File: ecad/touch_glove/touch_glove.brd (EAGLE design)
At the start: 78.3 x 40.6 mm, 173 parts, among them Q1 MCH3474 4A/30V, Q2 MCH3474 4A/30V, Q3 MCH3474 4A/30V, Q4 MCH3474 4A/30V, Q5 MCH3474 4A/30V, Q6 MCH3474 4A/30V, SW1 4A/28V, Y2 16 MHz

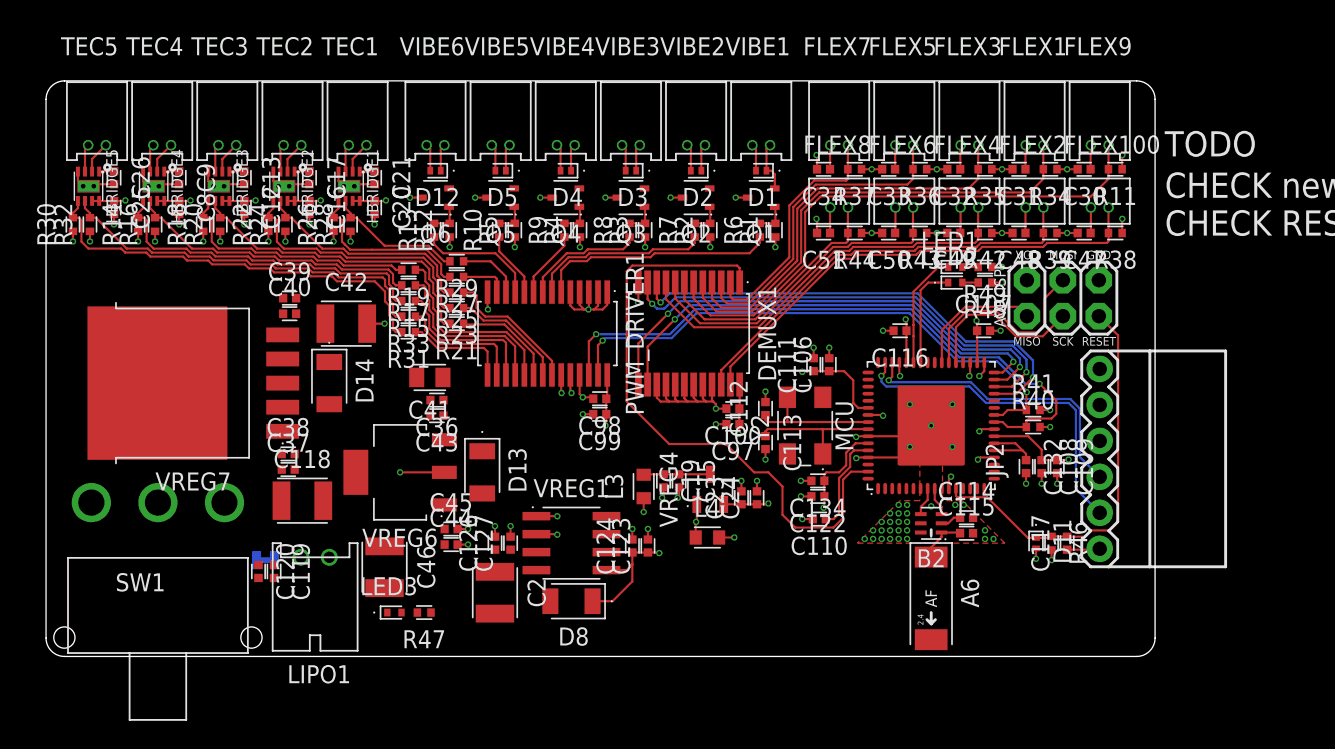
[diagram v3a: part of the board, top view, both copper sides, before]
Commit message: Add option to use two different analog voltages.
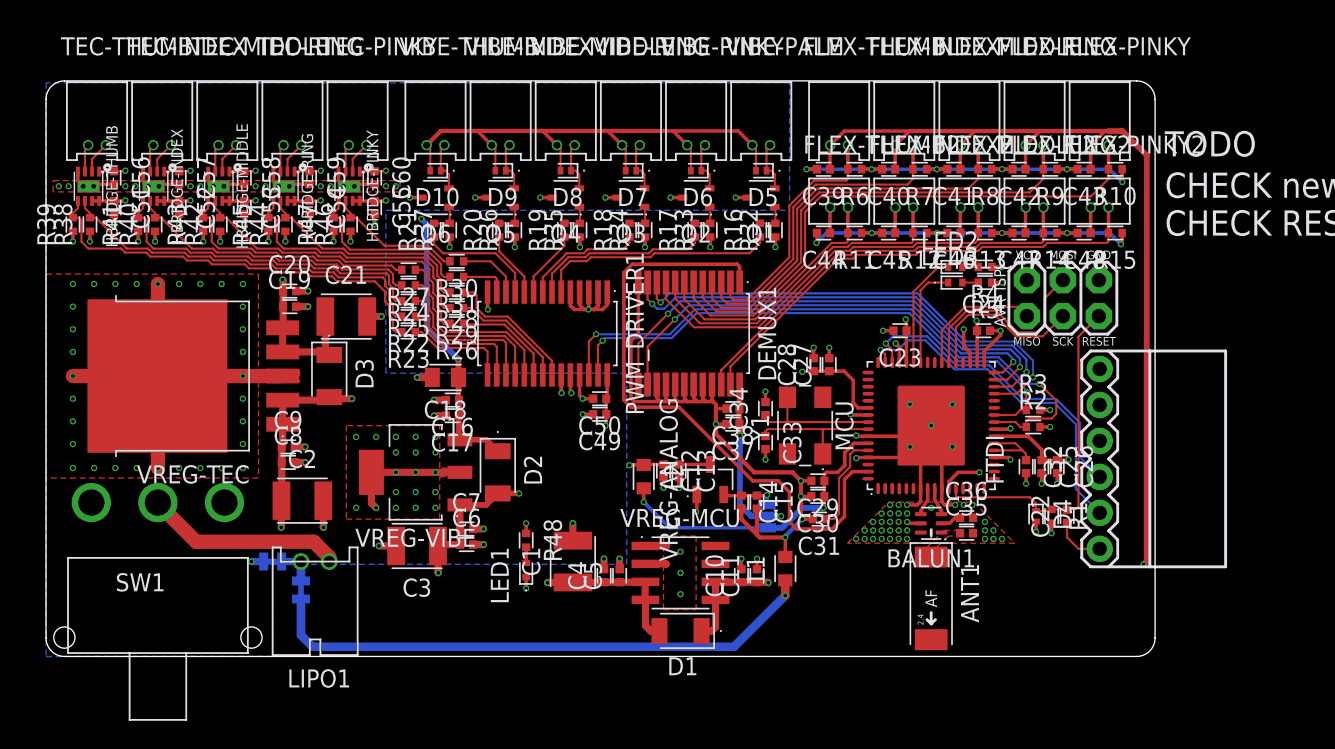
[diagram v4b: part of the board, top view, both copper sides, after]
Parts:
- removed C100, C108, C116, C117, C119, C122, C124, C127, C98: 0.1uF/50V, PiB_capacitors:CAPC1005X55_SMD-0402
- removed C107, C109, C110, C132: 1uF/25V, PiB_capacitors:CAPC1005X55_SMD-0402
- removed C112, C113: 12pF/100V, PiB_capacitors:CAPC1005X55_SMD-0402
- removed C114: 22pF/100V, PiB_capacitors:CAPC1005X55_SMD-0402
- removed C118: 100uF/16V, PiB_capacitors:CAPC3225X270_SMD-1210
- removed C120, C123, C126, C97, C99: 10uF/6.3V, PiB_capacitors:CAPC1005X55_SMD-0402
- removed D11: 150mA/75V, PiB_discrete_semiconductors:DFN100X60X55-2
- removed D13, D14: 1A/50V, PiB_discrete_semiconductors:SODFL3516X170
- removed L3, L4: 10uH/380mA, PiB_inductors:INDC1608X60
- removed NOISE_BR: 2PT_GND_TIE, PiB_power_symbols:2PT_GND_TIE
- removed R49: 1K, PiB_resistors:RESC1005X35
- removed VREG1: 1A/3.3V, PiB_ic_power:SOIC127P600X265-8
- removed VREG4: 250mA/3.3V, PiB_ic_power:SOT95P237X112-3_SOT-23-3
- removed VREG6: TL1963A-33 1.5A/3.3V, PiB_ic_power:SOT229P700X180-4
- removed VREG7: 3A/1.8V, PiB_ic_power:TO170P1363X457-6
- added BR_ANALOG, BR_NOISE: 2PT_GND_TIE, PiB_power_symbols:2PT_GND_TIE
- added C1, C3: 100uF/16V, PiB_capacitors:CAPC3225X270_SMD-1210
- added C10, C14, C22, C5, C52, C53, C54, C55, C56, C57, C58, C59, C60, C7: 0.1uF/50V, PiB_capacitors:CAPC1005X55_SMD-0402
- added C11, C4, C6: 10uF/6.3V, PiB_capacitors:CAPC1005X55_SMD-0402
- added C18: 47uF/6.3V, PiB_capacitors:CAPC2012X95_SMD-0805
- added D6, D7, D9: 150mA/75V, PiB_discrete_semiconductors:DFN100X60X55-2
- added JP1: JUMPER-SMT_3_NO_SILK, PiB_connectors:SMT-JUMPER_3_NO_SILK
- added L1, L2: 10uH/380mA, PiB_inductors:INDC1608X60
- added R45: 10KΩ, PiB_resistors:RESC1005X35
- added U$2: (no value), PiB_logo:MRSWIRLYEYES-LOGO
- added VREG-ANALOG: 250mA/3.3V, PiB_ic_power:SOT95P237X112-3_SOT-23-3
- added VREG-MCU: 1A/3.3V, PiB_ic_power:SOIC127P600X265-8
- added VREG-TEC: 3A/1.8V, PiB_ic_power:TO170P1363X457-6
- added VREG-VIBE: TL1963A-33 1.5A/3.3V, PiB_ic_power:SOT229P700X180-4
- C12, C15, C17, C20, C49, C8: value 0.1uF/50V -> 10uF/6.3V
- C19, C39, C43, C44: value 10uF/6.3V -> 0.1uF/50V
- C21: value 0.1uF/50V -> 100uF/16V; device PiB_capacitors:CAPC1005X55_SMD-0402 -> PiB_capacitors:CAPC3225X270_SMD-1210
- C24: value 10uF/6.3V -> 1uF/25V
- C26, C31, C32: value 0.1uF/50V -> 1uF/25V
- C33, C34: value 0.1uF/50V -> 12pF/100V
- C36: value 0.1uF/50V -> 22pF/100V
- C41: value 47uF/6.3V -> 0.1uF/50V; device PiB_capacitors:CAPC2012X95_SMD-0805 -> PiB_capacitors:CAPC1005X55_SMD-0402
- C42, C46: value 100uF/16V -> 0.1uF/50V; device PiB_capacitors:CAPC3225X270_SMD-1210 -> PiB_capacitors:CAPC1005X55_SMD-0402
- D1, D2, D3: value 150mA/75V -> 1A/50V; device PiB_discrete_semiconductors:DFN100X60X55-2 -> PiB_discrete_semiconductors:SODFL3516X170
- D8: value 1A/50V -> 150mA/75V; device PiB_discrete_semiconductors:SODFL3516X170 -> PiB_discrete_semiconductors:DFN100X60X55-2
- LED1: value GREEN -> BLUE
- LED2: value RED -> GREEN
- LED3: value BLUE -> RED
- R10, R13, R15, R6, R7, R8, R9: value 100 -> 47K
- R12, R14: value 10KΩ -> 47K
- R16, R18, R20, R22, R24, R26, R28, R30: value 10KΩ -> 100
- R2, R3: value 10KΩ -> 4.7K
- R33: value 100 -> 10KΩ
- R34, R35, R36, R37, R38, R39, R42, R43, R44: value 47K -> 10KΩ
- R4: value 10KΩ -> 1K
- R40, R41: value 4.7K -> 10KΩ
- R48: value 2K -> 10KΩ
- R5: value 10KΩ -> 2K
- U$1: device PiB_logo:MRSWIRLYEYES-LOGO -> PiB_logo:LRG-LOGO-2
- moved R38 72.4 mm to (3.10, 30.5), turned to 90 degrees
- moved C26 69.7 mm to (71.4, 13.4)
- moved R39 69.0 mm to (1.90, 30.5), turned to 90 degrees
- moved C25 68.0 mm to (70.3, 13.4)
- moved R41 64.5 mm to (6.50, 30.5), turned to 90 degrees
- moved R14 64.4 mm to (70.9, 29.9), turned to 180 degrees
- moved R40 63.6 mm to (7.70, 30.5), turned to 90 degrees
- moved R46 54.4 mm to (21.5, 30.5), turned to 90 degrees
- moved R42 54.0 mm to (12.3, 30.5), turned to 90 degrees
- moved R43 50.6 mm to (11.1, 30.5), turned to 90 degrees
- moved C51 50.1 mm to (4.80, 31.7), turned to 270 degrees
- moved R15 50.1 mm to (75.5, 29.9)
- moved C43 48.9 mm to (73.3, 34.4)
- moved C42 48.7 mm to (68.7, 34.4), turned to 180 degrees
- moved R32 48.4 mm to (51.5, 30.1)
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- renumbered A6 to ANT1, B2 to BALUN1, C106 to C27, C111 to C28, C115 to C35, C134 to C29, D12 to D10, FLEX1 to FLEX-RING, FLEX100 to FLEX-PINKY2, FLEX2 to FLEX-RING2, FLEX3 to FLEX-MIDDLE, FLEX4 to FLEX-MIDDLE2, FLEX5 to FLEX-INDEX, FLEX6 to FLEX-INDEX2, FLEX7 to FLEX-THUMB, FLEX8 to FLEX-THUMB2, FLEX9 to FLEX-PINKY, HBRIDGE1 to HBRIDGE-PINKY, HBRIDGE2 to HBRIDGE-RING, HBRIDGE3 to HBRIDGE-MIDDLE, HBRIDGE4 to HBRIDGE-INDEX, HBRIDGE5 to HBRIDGE-THUMB, JP2 to FTDI, TEC1 to TEC-PINKY, TEC2 to TEC-RING, TEC3 to TEC-MIDDLE, TEC4 to TEC-INDEX, TEC5 to TEC-THUMB, VIBE1 to VIBE-PALM, VIBE2 to VIBE-PINKY, VIBE3 to VIBE-RING, VIBE4 to VIBE-MIDDLE, VIBE5 to VIBE-INDEX, VIBE6 to VIBE-THUMB, Y2 to Y1
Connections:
- net N$49 renamed RFSIG
- removed net STRAIN_1: DEMUX1.5, FLEX-RING.2, R34.2
- removed net STRAIN_10: DEMUX1.23, FLEX-PINKY2.2, R38.2
- removed net STRAIN_2: DEMUX1.22, FLEX-RING2.2, R39.2
- removed net STRAIN_3: DEMUX1.4, FLEX-MIDDLE.2, R35.2
- removed net STRAIN_4: DEMUX1.9, FLEX-MIDDLE2.2, R42.2
- removed net STRAIN_5: DEMUX1.3, FLEX-INDEX.2, R36.2
- removed net STRAIN_6: DEMUX1.8, FLEX-INDEX2.2, R43.2
- removed net STRAIN_7: DEMUX1.2, FLEX-THUMB.2, R37.2
- removed net STRAIN_8: DEMUX1.7, FLEX-THUMB2.2, R44.2
- removed net STRAIN_9: DEMUX1.6, FLEX-PINKY.2, R11.2
- removed net TEC_1_COLD: PWM_DRIVER1.13, R27.1
- removed net TEC_1_HOT: PWM_DRIVER1.12, R29.1
- removed net TEC_2_COLD: PWM_DRIVER1.21, R23.1
- removed net TEC_2_HOT: PWM_DRIVER1.22, R25.1
- removed net TEC_3_COLD: PWM_DRIVER1.19, R19.1
- removed net TEC_3_HOT: PWM_DRIVER1.20, R21.1
- removed net TEC_4_COLD: PWM_DRIVER1.17, R15.1
- removed net TEC_4_HOT: PWM_DRIVER1.18, R17.1
- removed net TEC_5_COLD: PWM_DRIVER1.15, R31.1
- removed net TEC_5_HOT: PWM_DRIVER1.16, R33.1
- removed net VIBE_1: PWM_DRIVER1.6, R6.1
- removed net VIBE_2: PWM_DRIVER1.7, R7.1
- removed net VIBE_3: PWM_DRIVER1.8, R8.1
- removed net VIBE_4: PWM_DRIVER1.9, R9.1
- removed net VIBE_5: PWM_DRIVER1.10, R10.1
- removed net VIBE_6: PWM_DRIVER1.11, R13.1
- new net FLEX-INDEX1: DEMUX1.3, FLEX-INDEX.2, R7.2
- new net FLEX-INDEX2: DEMUX1.8, FLEX-INDEX2.2, R12.2
- new net FLEX-MIDDLE1: DEMUX1.4, FLEX-MIDDLE.2, R8.2
- new net FLEX-MIDDLE2: DEMUX1.9, FLEX-MIDDLE2.2, R13.2
- new net FLEX-PINKY1: DEMUX1.6, FLEX-PINKY.2, R10.2
- new net FLEX-PINKY2: DEMUX1.23, FLEX-PINKY2.2, R15.2
- new net FLEX-RING1: DEMUX1.5, FLEX-RING.2, R9.2
- new net FLEX-RING2: DEMUX1.22, FLEX-RING2.2, R14.2
- new net FLEX-THUMB1: DEMUX1.2, FLEX-THUMB.2, R6.2
- new net FLEX-THUMB2: DEMUX1.7, FLEX-THUMB2.2, R11.2
- new net N$40: BR_ANALOG.P$2, L1.1
- new net TEC-INDEX-COLD: PWM_DRIVER1.17, R25.1
- new net TEC-INDEX-HOT: PWM_DRIVER1.18, R24.1
- new net TEC-MIDDLE-COLD: PWM_DRIVER1.19, R27.1
- new net TEC-MIDDLE-HOT: PWM_DRIVER1.20, R26.1
- new net TEC-PINKY-COLD: PWM_DRIVER1.13, R31.1
- new net TEC-PINKY-HOT: PWM_DRIVER1.12, R30.1
- new net TEC-RING-COLD: PWM_DRIVER1.21, R29.1
- new net TEC-RING-HOT: PWM_DRIVER1.22, R28.1
- new net TEC-THUMB-COLD: PWM_DRIVER1.15, R23.1
- new net TEC-THUMB-HOT: PWM_DRIVER1.16, R22.1
- new net VIBE-INDEX: PWM_DRIVER1.10, R20.1
- new net VIBE-MIDDLE: PWM_DRIVER1.9, R19.1
- new net VIBE-PALM: PWM_DRIVER1.6, R16.1
- new net VIBE-PINKY: PWM_DRIVER1.7, R17.1
- new net VIBE-RING: PWM_DRIVER1.8, R18.1
- new net VIBE-THUMB: PWM_DRIVER1.11, R21.1
- new net VSENSOR: C37.1, C38.1, C39.1, C40.1, C41.1, C42.1, C43.1, C44.1, C45.1, C46.1, C47.1, C48.1, DEMUX1.24, FLEX-INDEX.1, FLEX-INDEX2.1, FLEX-MIDDLE.1, FLEX-MIDDLE2.1, FLEX-PINKY.1, FLEX-PINKY2.1, FLEX-RING.1, FLEX-RING2.1, FLEX-THUMB.1, FLEX-THUMB2.1, JP1.2
- net +: now also SW1.P; no longer SW1.S1
- net 1.8V: now also C19.1, C20.1, C56.1, C57.1, C58.1, C59.1, C60.1, D3.A, VREG-TEC.4, VREG-TEC.5; no longer C13.1, C17.1, C26.1, C39.1, C40.1, C42.1, C9.1, D14.A, VREG7.4, VREG7.5
- net 3.3V: now also C16.1, C17.1, C18.1, D2.A, D6.K, D7.K, D8.K, D9.K, VREG-VIBE.3; no longer C36.1, C41.1, C43.1, D1.K, D13.A, D2.K, D3.K, D4.K, VREG6.3
- net AGND: now also C14.2, C15.2, C36.2, C37.2, C38.2, C39.2, C40.2, C41.2, C42.2, C43.2, C44.2, C45.2, C46.2, L1.2, R10.1, R12.1, R13.1, R14.1, R15.1, R6.1, R7.1, R8.1, R9.1; no longer C100.2, C110.2, C114.2, C122.2, C23.2, C24.2, C32.2, C33.2, C34.2, C49.2, C50.2, C51.2, C97.2, L4.2, R34.1, R35.1, R36.1, R37.1, R38.1, R39.1, R42.1, R43.1, R44.1
- net AVCC: now also JP1.3, L2.2; no longer C100.1, C122.1, C23.1, C24.1, C31.1, C32.1, C33.1, C34.1, C47.1, C48.1, C49.1, C50.1, C51.1, C97.1, DEMUX1.24, FLEX-INDEX.1, FLEX-INDEX2.1, FLEX-MIDDLE.1, FLEX-MIDDLE2.1, FLEX-PINKY.1, FLEX-PINKY2.1, FLEX-RING.1, FLEX-RING2.1, FLEX-THUMB.1, FLEX-THUMB2.1, VREG4.2
- net GND: now also BR_ANALOG.P$1, BR_NOISE.P$2, C10.2, C11.2, C13.2, C23.2, C24.2, C26.2, C32.2, C33.2, C34.2, C49.2, C50.2, C51.2, C52.2, C53.2, C54.2, C55.2, R33.1, R34.1, R35.1, R36.1, R37.1, R38.1, R39.1, R40.1, R41.1, R42.1, R43.1, R44.1, R45.1, R46.1, VREG-ANALOG.1, VREG-MCU.1, VREG-MCU.2; no longer C107.2, C108.2, C109.2, C112.2, C113.2, C116.2, C118.2, C119.2, C120.2, C123.2, C124.2, C126.2, C127.2, C132.2, C15.2, C16.2, C19.2, C2.2, C20.2, C37.2, C38.2, C44.2, C45.2, C46.2, C8.2, C98.2, C99.2, L4.1, NOISE_BR.P$2, R1.1, R12.1, R14.1, R16.1, R18.1, R2.1, R20.1, R22.1, R24.1, R26.1, R28.1, R3.1, R30.1, R48.1, R49.1, VREG1.1, VREG1.2, VREG4.1
- net N$10: now also R24.2, R40.2; no longer R16.2, R17.2
- net N$13: now also R27.2, R43.2; no longer R18.2, R19.2
- net N$14: now also R26.2, R42.2; no longer R20.2, R21.2
- net N$15: now also D6.A; no longer D2.A
- net N$17: now also D5.A; no longer D1.A
- net N$19: now also R29.2, R45.2; no longer R22.2, R23.2
- net N$2: now also D8.A; no longer D4.A
- net N$20: now also R28.2, R44.2; no longer R24.2, R25.2
- net N$21: now also R19.2, R35.2; no longer R4.2, R9.2
- net N$22: now also R20.2, R36.2; no longer R10.2, R5.2
- net N$25: now also R31.2, R47.2; no longer R26.2, R27.2
- net N$26: now also R30.2, R46.2; no longer R28.2, R29.2
- net N$28: now also R16.2, R32.2; no longer R1.2, R6.2
- net N$29: now also R23.2, R39.2; no longer R30.2, R31.2
- net N$3: now also D9.A; no longer D5.A
- net N$31: now also R22.2, R38.2; no longer R32.2, R33.2
- net N$32: now also R21.2, R37.2; no longer R12.2, R13.2
- net N$33: now also C14.1, JP1.1, VREG-ANALOG.2; no longer C19.1, L3.2, VREG4.3
- net N$35: now also C34.1; no longer C112.1
- net N$36: now also C33.1; no longer C113.1
- net N$4: now also D7.A; no longer D3.A
- net N$47: now also C36.1; no longer C114.1
- net N$50: now also C22.1; no longer C117.1
- net N$53: now also LED1.K, R48.2; no longer LED3.K, R47.2
- net N$54: now also LED2.K, R4.2; no longer LED1.K, R49.2
- net N$55: now also LED3.K, R5.2; no longer LED2.K, R48.2
- net N$62: now also C32.1; no longer C132.1
- net N$63: now also C31.1; no longer C110.1
- net N$7: now also R17.2, R33.2; no longer R2.2, R7.2
- net N$8: now also R25.2, R41.2; no longer R14.2, R15.2
- net N$9: now also R18.2, R34.2; no longer R3.2, R8.2
- net NGND: now also BR_NOISE.P$1, C1.2, C16.2, C18.2, C19.2, C2.2, C20.2, C3.2, C4.2, C5.2, C56.2, C57.2, C58.2, C59.2, C6.2, C60.2, C7.2, C8.2, R48.1, VREG-TEC.3, VREG-TEC.6, VREG-VIBE.2, VREG-VIBE.4; no longer C13.2, C26.2, C36.2, C39.2, C40.2, C41.2, C42.2, C43.2, NOISE_BR.P$1, VREG6.2, VREG6.4, VREG7.3, VREG7.6
- net PB6: now also LED3.A; no longer LED2.A
- net PB7: now also LED2.A; no longer LED1.A
- net RESET: now also C22.2, D4.A, R1.1; no longer C117.2, D11.A, R46.1
- net SCL: now also R2.1; no longer R40.1
- net SDA: now also R3.1; no longer R41.1
- net VBATT: now also C1.1, C3.1, C4.1, C5.1, C6.1, C7.1, C8.1, C9.1, D1.K, D2.K, D3.K, LED1.A, SW1.S1, VREG-MCU.3, VREG-MCU.4, VREG-TEC.1, VREG-TEC.2, VREG-VIBE.1; no longer C118.1, C119.1, C120.1, C126.1, C127.1, C37.1, C38.1, C44.1, C45.1, C46.1, D13.K, D14.K, D8.K, LED3.A, SW1.P, VREG1.3, VREG1.4, VREG6.1, VREG7.1, VREG7.2
- net VCC: now also C10.1, C11.1, C13.1, C23.1, C24.1, C26.1, C49.1, C50.1, C51.1, C52.1, C53.1, C54.1, C55.1, D1.A, D4.K, L2.1, R1.2, R2.2, R3.2, VREG-ANALOG.3, VREG-MCU.5, VREG-MCU.6; no longer C107.1, C108.1, C109.1, C116.1, C123.1, C124.1, C16.1, C20.1, C8.1, C98.1, C99.1, D11.K, D8.A, L3.1, R40.2, R41.2, R46.2, VREG1.5, VREG1.6
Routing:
- net AGND: track 48.8 -> 210.0 mm, vias 49 -> 54
- net VSENSOR: track 0.00 -> 154.8 mm, vias 0 -> 3
- net 3.3V: track 11.4 -> 66.3 mm, vias 0 -> 2
- net NGND: track 22.8 -> 73.0 mm, vias 8 -> 86
- net N$40: track 0.00 -> 39.7 mm, vias 0 -> 1
- net STRAIN_9: track 39.4 -> 0.00 mm
- net FLEX-PINKY1: track 0.00 -> 39.4 mm
- net VBATT: track 0.00 -> 36.9 mm, vias 0 -> 6
- net STRAIN_10: track 34.0 -> 0.00 mm
- net FLEX-PINKY2: track 0.00 -> 34.0 mm
- net STRAIN_1: track 33.9 -> 0.00 mm
- net FLEX-RING1: track 0.00 -> 33.9 mm
- net STRAIN_2: track 29.9 -> 0.00 mm
- net FLEX-RING2: track 0.00 -> 29.9 mm
- net STRAIN_4: track 28.9 -> 0.00 mm
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- added copper zone on layer 2, net 1.8V
- added copper zone on layer 1, net GND
- added copper zone on layer 2, net N$37
- added copper zone on layer 1, net NGND
- added copper zone on layer 16, net NGND
- added copper zone on layer 1, net RFSIG
- added copper zone on layer 2, net VBATT
- removed copper zone on layer 2, net AGND
- removed copper zone on layer 2, net AVCC
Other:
- board text added: "Designed by: &"
- board text added: "MrSwirlyEyes"
- board text removed: "Designed by: MrSwirlyEyes"

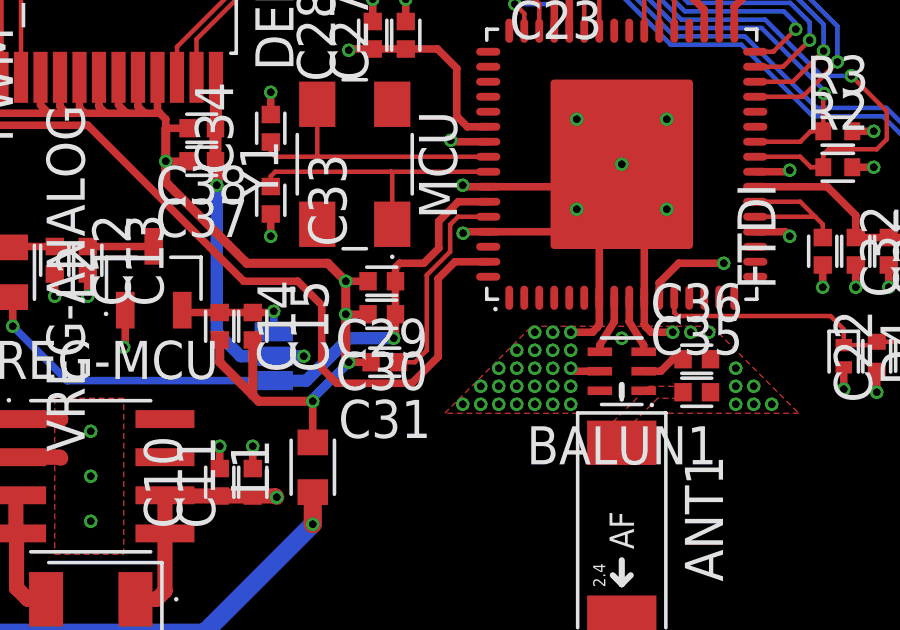
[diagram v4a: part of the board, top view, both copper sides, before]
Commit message: Replaced Robotic Arm components for those with 3D models.  Also went down to 0402 component size.
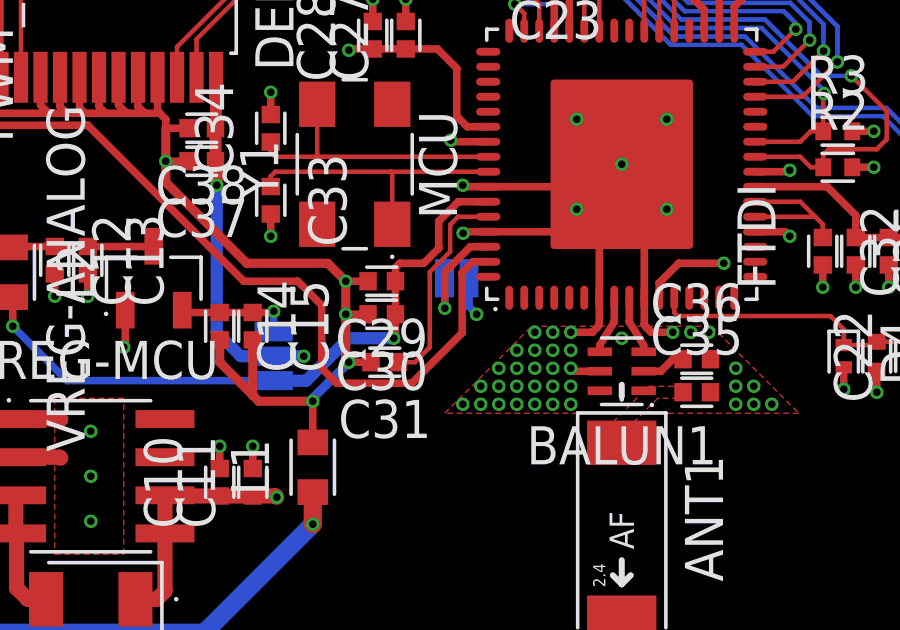
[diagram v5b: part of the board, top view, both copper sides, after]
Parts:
- added JP2: JUMPER-SMT_2_NO_SILK, PiB_connectors:SMT-JUMPER_2_NO_SILK
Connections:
- new net N$39: JP2.2, MCU.62
- net VSENSOR: now also JP2.1
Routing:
- net N$39: track 0.00 -> 4.00 mm, vias 0 -> 1
- net VSENSOR: track 154.8 -> 157.4 mm, vias 3 -> 4
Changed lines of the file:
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@@
 </layers>
 <board>
-<fusionsync huburn="a.cGVyc29uYWw6dWUyOTIwMzJm" projecturn="a.cGVyc29uYWw6dWUyOTIwMzJmIzIwMTYwNDI5MzA4MDY3NTY" f3durn="urn:adsk.wipprod:dm.lineage:dZKVV2TOQ-GfPmiZokfcDw" pcbguid="55b963d9-4c6d-479b-bd22-0a896272d867" lastpulledtime="" lastsyncedchangeguid="c83149b8-2998-94a7-ed76-f1967327cd56"/>
+<fusionsync huburn="a.cGVyc29uYWw6dWUyOTIwMzJm" projecturn="a.cGVyc29uYWw6dWUyOTIwMzJmIzIwMTYwNDI5MzA4MDY3NTY" f3durn="urn:adsk.wipprod:dm.lineage:dZKVV2TOQ-GfPmiZokfcDw" pcbguid="55b963d9-4c6d-479b-bd22-0a896272d867" lastpulledtime="" lastsyncedchangeguid="f1565c9e-5985-66dc-efcc-659af679d701"/>
 <plain>
 <wire x1="77.0072" y1="40.64" x2="1.3008" y2="40.64" width="0" layer="20"/>
@@
 <element name="U$2" library="PiB_logo" package="MRSWIRLYEYES-LOGO" value="" x="43" y="8" rot="MR0"/>
 <element name="JP1" library="PiB_connectors" library_urn="urn:adsk.eagle:library:2993000" package="SMT-JUMPER_3_NO_SILK" package3d_urn="urn:adsk.eagle:package:2993085/1" value="JUMPER-SMT_3_NO_SILK" x="50.9" y="9.9" rot="MR270"/>
+<element name="JP2" library="PiB_connectors" package="SMT-JUMPER_2_NO_SILK" value="JUMPER-SMT_2_NO_SILK" x="57" y="12.5" rot="MR0"/>
 </elements>
 <signals>
@@
 <contactref element="MCU" pad="63"/>
 <contactref element="DEMUX1" pad="1"/>
-<wire x1="58.0494" y1="13.05" x2="56.940275" y2="13.05" width="0.254" layer="1"/>
-<wire x1="56.940275" y1="13.05" x2="56.3794" y2="12.489125" width="0.254" layer="1"/>
-<wire x1="56.3794" y1="9.8794" x2="55.5" y2="9" width="0.254" layer="1"/>
+<wire x1="58.0494" y1="13.05" x2="57.540275" y2="13.05" width="0.254" layer="1"/>
+<wire x1="57.540275" y1="13.05" x2="57.1794" y2="12.689125" width="0.254" layer="1"/>
+<wire x1="57.1794" y1="10.6794" x2="55.5" y2="9" width="0.254" layer="1"/>
 <wire x1="52.5" y1="9.5" x2="53" y2="9" width="0.254" layer="1"/>
-<wire x1="56.3794" y1="12.489125" x2="56.3794" y2="9.8794" width="0.254" layer="1"/>
+<wire x1="57.1794" y1="12.689125" x2="57.1794" y2="10.6794" width="0.254" layer="1"/>
 <wire x1="55.5" y1="9" x2="53" y2="9" width="0.254" layer="1"/>
 <wire x1="40.8" y1="27.1" x2="40.8" y2="18.1" width="0.254" layer="1"/>
@@
 <wire x1="56.7794" y1="14.2842625" x2="57.0451375" y2="14.55" width="0.1524" layer="1"/>
 <wire x1="56.7794" y1="14.2842625" x2="56.7794" y2="13.3842625" width="0.1524" layer="1"/>
-<wire x1="56" y1="12.6048625" x2="56.7794" y2="13.3842625" width="0.1524" layer="1"/>
+<wire x1="56.1" y1="12.7048625" x2="56.7794" y2="13.3842625" width="0.1524" layer="1"/>
 <wire x1="55.0575" y1="9.7" x2="55.6" y2="9.7" width="0.1524" layer="1"/>
-<wire x1="55.6" y1="9.7" x2="56" y2="10.1" width="0.1524" layer="1"/>
-<wire x1="56" y1="10.1" x2="56" y2="12.6048625" width="0.1524" layer="1"/>
+<wire x1="55.6" y1="9.7" x2="56.1" y2="10.2" width="0.1524" layer="1"/>
+<wire x1="56.1" y1="10.2" x2="56.1" y2="12.7048625" width="0.1524" layer="1"/>
 </signal>
 <signal name="FLEX-INDEX2">
@@
 <wire x1="51.9" y1="9.9" x2="53.4" y2="8.4" width="0.4064" layer="2"/>
 <wire x1="53.4" y1="8.4" x2="56.1" y2="8.4" width="0.4064" layer="2"/>
-<wire x1="56.1" y1="8.4" x2="59.7" y2="12" width="0.4064" layer="2"/>
+<wire x1="56.1" y1="8.4" x2="57.65" y2="9.95" width="0.4064" layer="2"/>
+<wire x1="57.65" y1="9.95" x2="59.7" y2="12" width="0.4064" layer="2"/>
 <wire x1="59.7" y1="19.2" x2="60.1" y2="19.6" width="0.4064" layer="2"/>
 <wire x1="59.7" y1="12" x2="59.7" y2="19.2" width="0.4064" layer="2"/>
@@
 <wire x1="69.175" y1="31.7" x2="69.175" y2="36.1" width="0.254" layer="2"/>
 <wire x1="69.175" y1="36.1" x2="70.175" y2="37.1" width="0.254" layer="1"/>
+<contactref element="JP2" pad="1"/>
+<wire x1="57.4064" y1="12.5" x2="57.4064" y2="11.5556" width="0.254" layer="16"/>
+<wire x1="57.4064" y1="11.5556" x2="57.662" y2="11.3" width="0.254" layer="16"/>
+<via x="57.662" y="11.3" extent="1-16" drill="0.254"/>
+<wire x1="57.662" y1="11.3" x2="57.662" y2="9.962" width="0.254" layer="2"/>
+<wire x1="57.662" y1="9.962" x2="57.65" y2="9.95" width="0.254" layer="2"/>
+</signal>
+<signal name="N$39">
+<contactref element="JP2" pad="2"/>
+<contactref element="MCU" pad="62"/>
+<via x="56.6" y="11.5" extent="1-16" drill="0.254"/>
+<wire x1="58.0494" y1="13.55" x2="57.45" y2="13.55" width="0.254" layer="1"/>
+<wire x1="56.6" y1="12.7" x2="56.6" y2="11.5" width="0.254" layer="1"/>
+<wire x1="57.45" y1="13.55" x2="56.6" y2="12.7" width="0.254" layer="1"/>
+<wire x1="56.5936" y1="12.5" x2="56.6" y2="12.4936" width="0.254" layer="16"/>
+<wire x1="56.6" y1="12.4936" x2="56.6" y2="11.5" width="0.254" layer="16"/>
 </signal>
 </signals>
